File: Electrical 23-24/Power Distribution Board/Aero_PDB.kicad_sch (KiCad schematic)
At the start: 8 parts, among them J101 Conn_02x13_Top_Bottom

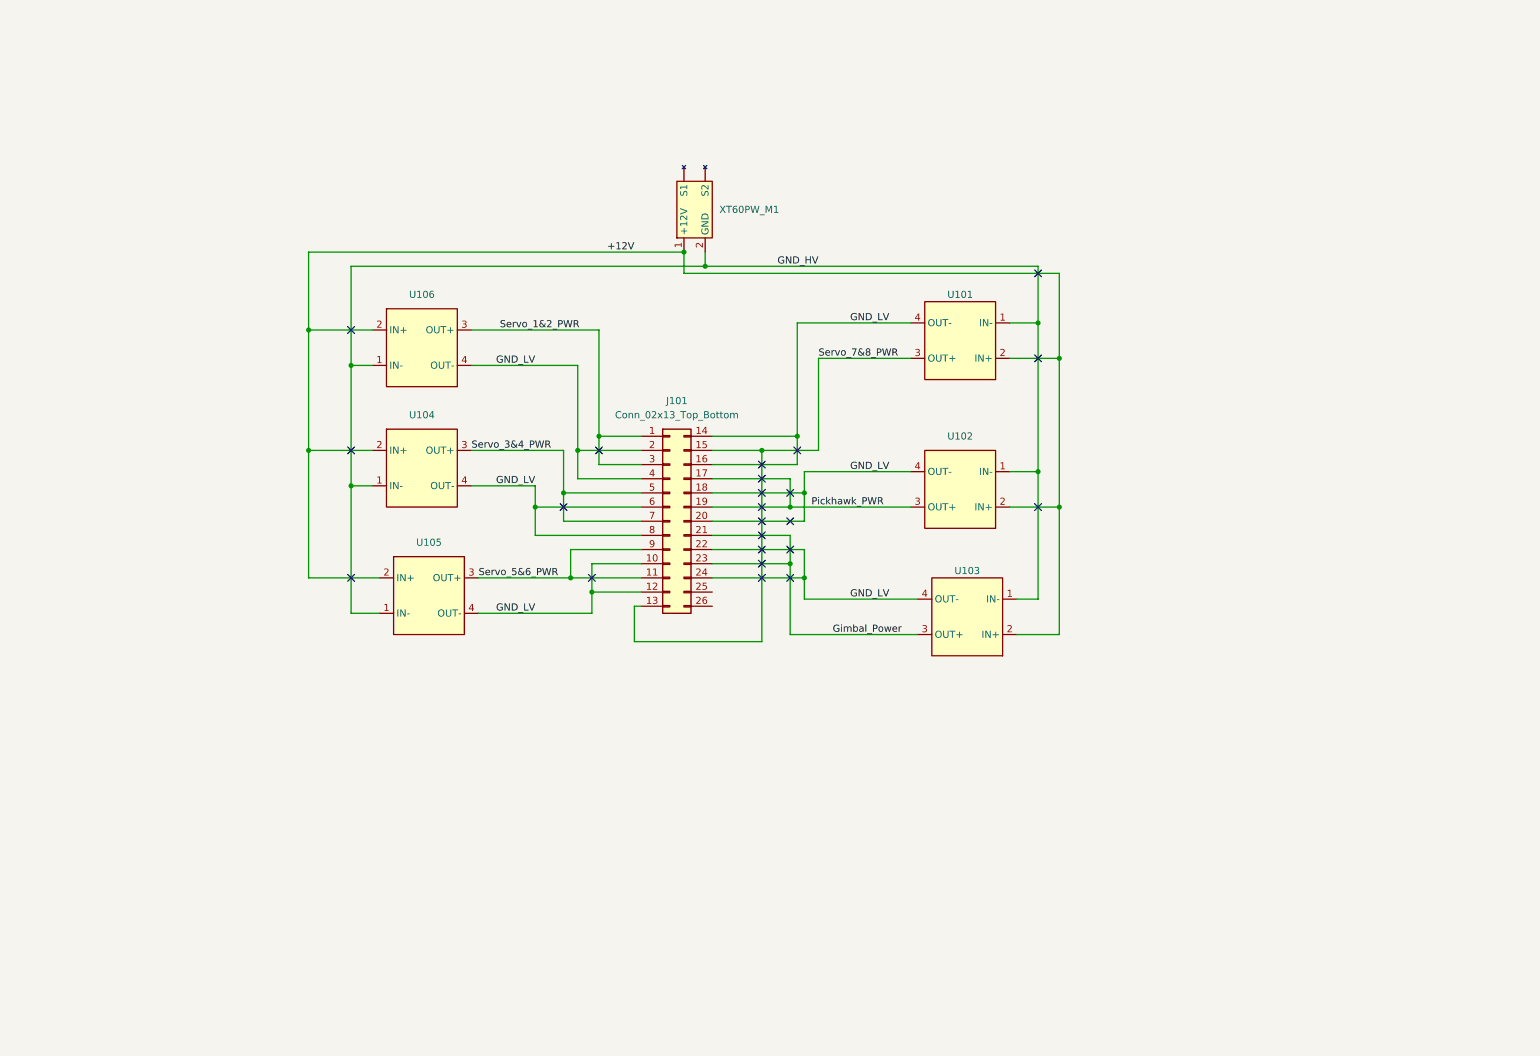
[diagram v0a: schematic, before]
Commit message: Updates to the PDB Design
Pushed Some Buck Converters to the back 
Added more connectors (for RasPi, Bullet, etc.)
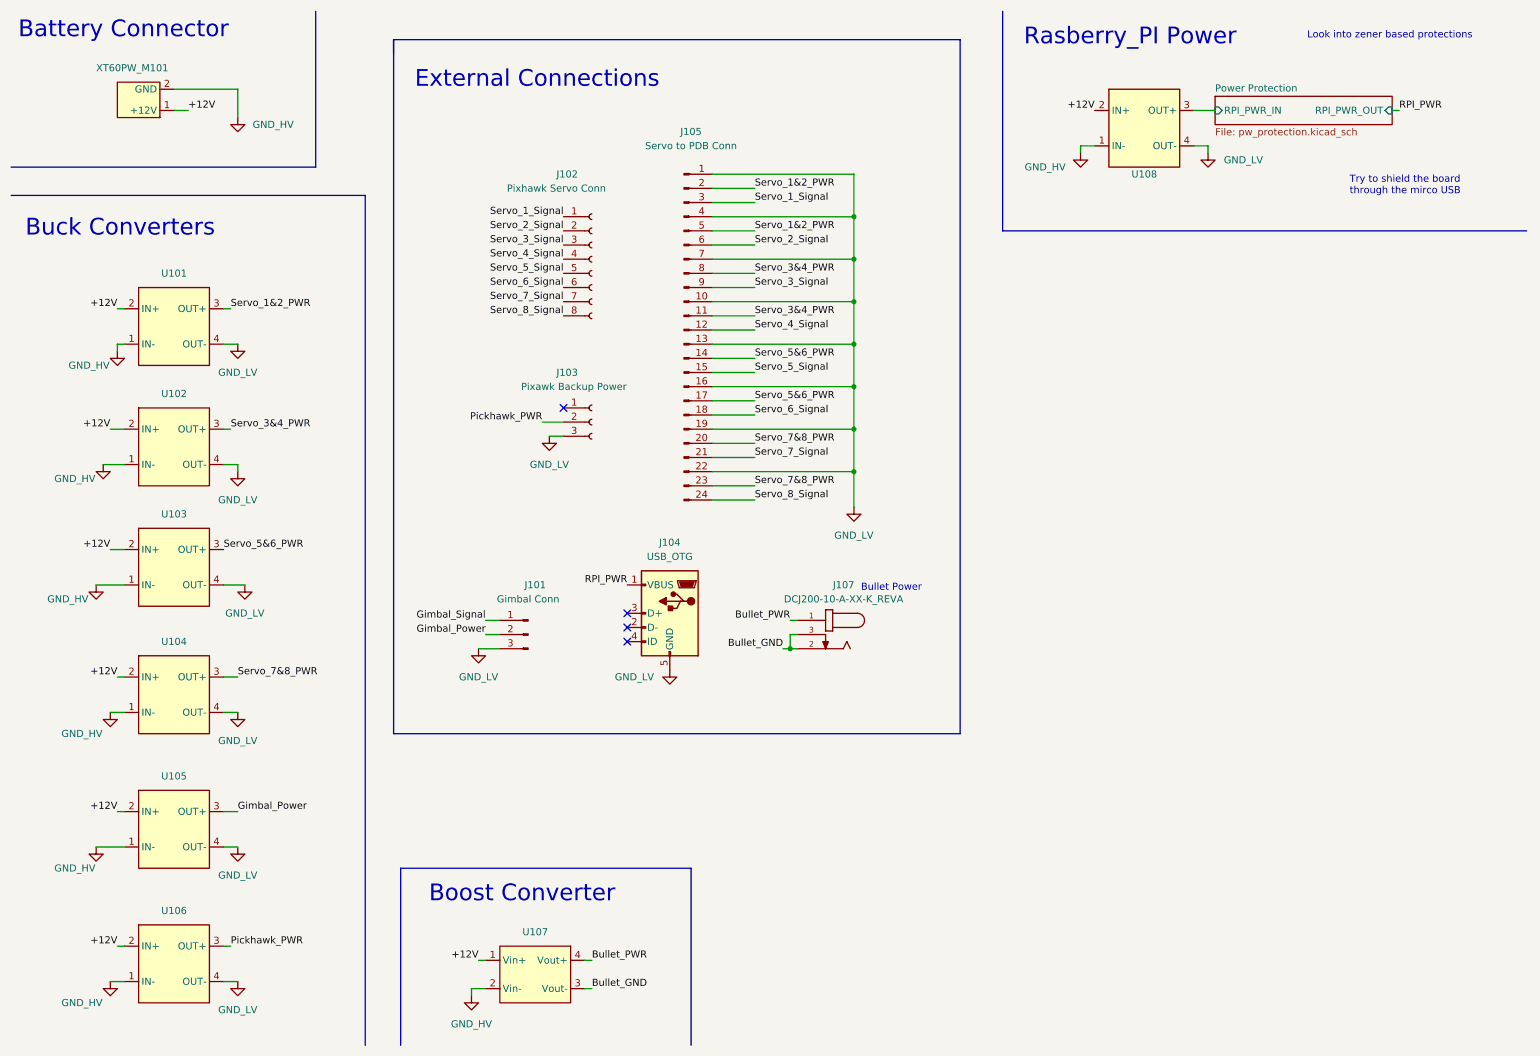
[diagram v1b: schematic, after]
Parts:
- removed J101: Conn_02x13_Top_Bottom, Connector_PinHeader_2.54mm:PinHeader_2x13_P2.54mm_Horizontal, symbol Connector_Generic:Conn_02x13_Top_Bottom
- added J101: Gimbal Conn, Connector_JST:JST_EH_B3B-EH-A_1x03_P2.50mm_Vertical, symbol Connector:Conn_01x03_Pin
- added J102: Pixhawk Servo Conn, Aero_PDB:CONN8_LFBN-RC_SUL, symbol Connector:Conn_01x08_Socket
- added J103: Pixawk Backup Power, Aero_PDB:SAMTEC_DW-03-XX-X-S-XXX, symbol Connector:Conn_01x03_Socket
- added J104: USB_OTG, Aero_PDB:MOLEX_47346-0001, symbol Connector:USB_OTG
- added J105: Servo to PDB Conn, Aero_PDB:SAMTEC_TSW-108-08-L-T-RA, symbol Connector:Conn_01x24_Pin
- added J107: DCJ200-10-A-XX-K_REVA, Aero_PDB:GCT_DCJ200-10-A-XX-K_REVA, symbol Aero_PDB_parts:DCJ200-10-A-XX-K_REVA
- added U107: ~, Aero_PDB:MT3608_module, symbol Aero_PDB_parts:MT3608_Boost_
- added U108: ~, Aero_PDB:YAAJ_DCDC_StepDown_LM2596, symbol Aero_PDB_parts:LM2596
- renumbered U106 to U101, U104 to U102, U105 to U103, U101 to U104, U103 to U105, U102 to U106, XT60PW_M1 to XT60PW_M101
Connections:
- net GND_LV is gone; now on net GND: U101.4 (OUT-), U102.4 (OUT-), U103.4 (OUT-), U104.4 (OUT-), U105.4 (OUT-), U106.4 (OUT-)
- net +12V: now also U107.1 (Vin+), U108.2 (IN+)
- net Gimbal_Power: now also J101.2 (Pin_2)
- net Pickhawk_PWR: now also J103.2 (Pin_2)
- net Servo_1&2_PWR: now also J105.2 (Pin_2), J105.5 (Pin_5)
- net Servo_3&4_PWR: now also J105.11 (Pin_11), J105.8 (Pin_8)
- net Servo_5&6_PWR: now also J105.14 (Pin_14), J105.17 (Pin_17)
- net Servo_7&8_PWR: now also J105.20 (Pin_20), J105.23 (Pin_23)
- net GND_HV renamed GND
- net GND: now also J101.3 (Pin_3), J104.5 (GND), J105.1 (Pin_1), J105.10 (Pin_10), J105.13 (Pin_13), J105.16 (Pin_16), J105.19 (Pin_19), J105.22 (Pin_22), J105.4 (Pin_4), J105.7 (Pin_7), U107.2 (Vin-), U108.4 (OUT-)
- new net Bullet_GND : J107.2, J107.3, U107.3 (Vout-)
- new net Bullet_PWR: J107.1, U107.4 (Vout+)
- new net GND1: U108.1 (IN-)
- new net GND2: J103.3 (Pin_3)
- new net Gimbal_Signal: J101.1 (Pin_1)
- new net Power Protection /RPI_PWR_IN: U108.3 (OUT+)
- new net RPI_PWR: J104.1 (VBUS)
- new net Servo_1_Signal: J102.1 (Pin_1), J105.3 (Pin_3)
- new net Servo_2_Signal: J102.2 (Pin_2), J105.6 (Pin_6)
- new net Servo_3_Signal: J102.3 (Pin_3), J105.9 (Pin_9)
- new net Servo_4_Signal: J102.4 (Pin_4), J105.12 (Pin_12)
- new net Servo_5_Signal: J102.5 (Pin_5), J105.15 (Pin_15)
- new net Servo_6_Signal: J102.6 (Pin_6), J105.18 (Pin_18)
- new net Servo_7_Signal: J102.7 (Pin_7), J105.21 (Pin_21)
- new net Servo_8_Signal: J102.8 (Pin_8), J105.24 (Pin_24)
- no-connect marks 23 -> 4
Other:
- added sheet Power Protection  (pw_protection.kicad_sch)
- note added: "Battery Connector"
- note added: "Boost Converter"
- note added: "Buck Converters"
- note added: "Bullet Power"
- note added: "External Connections"
- note added: "Look into zener based protections"
- note added: "Rasberry_PI Power"
- note added: "Try to shield the board through the mirco USB"
- moved on the sheet: U101, U102, U103, U104, U105, U106

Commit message: Final PDB (missing Aero Logo)
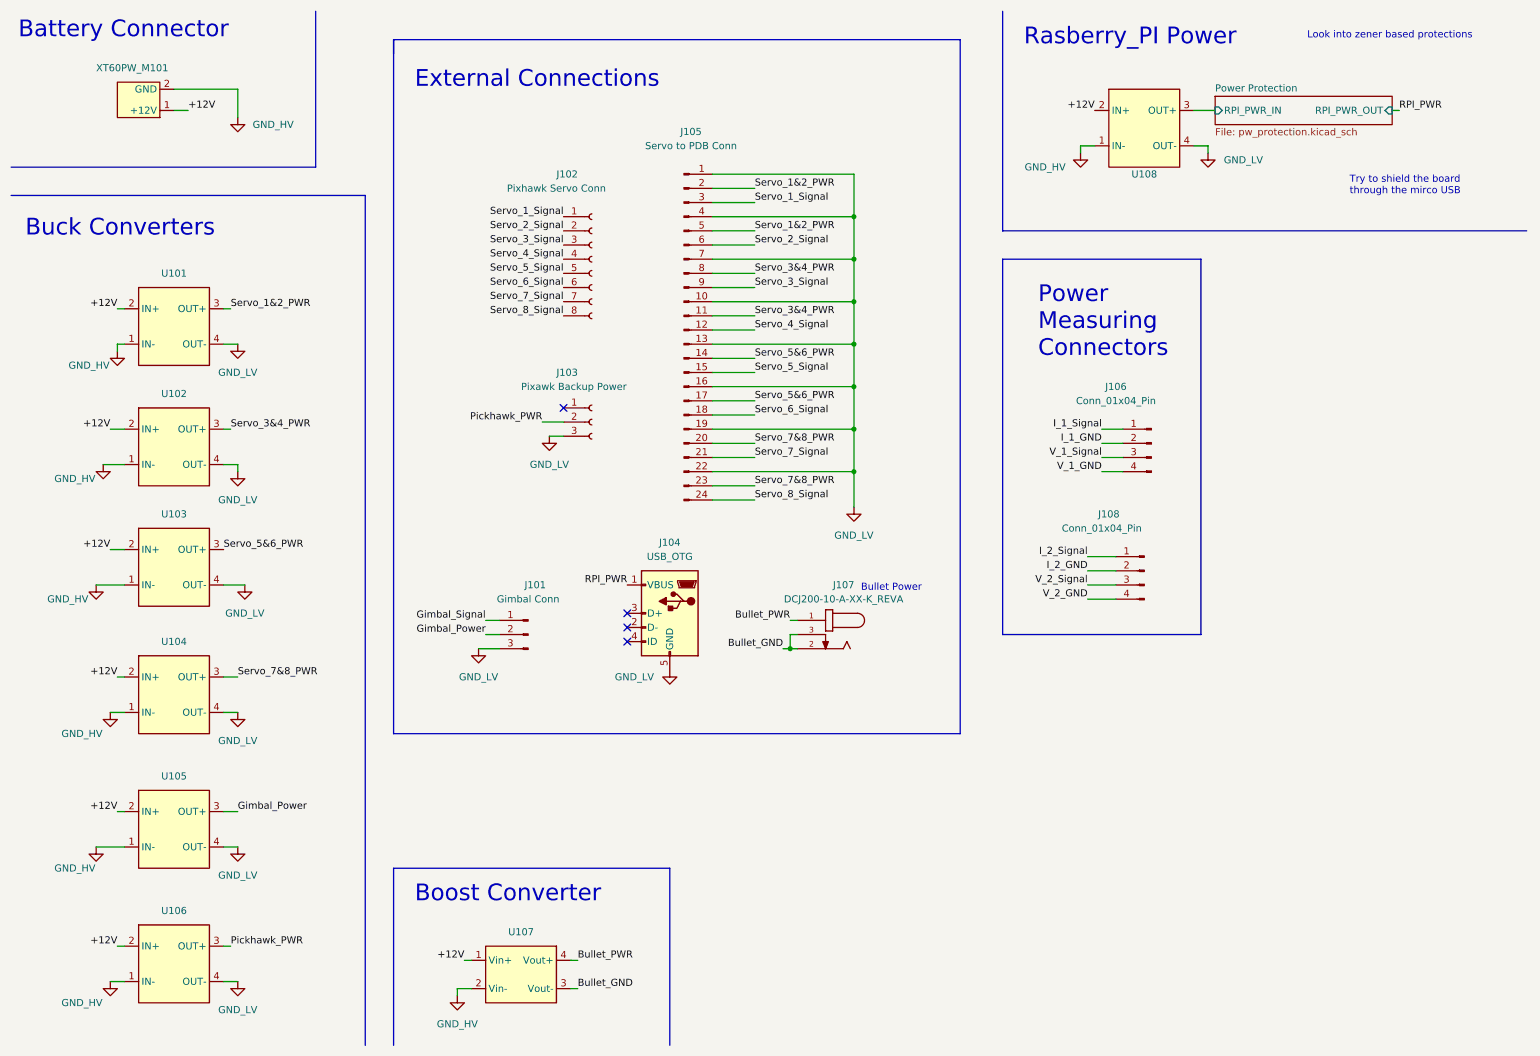
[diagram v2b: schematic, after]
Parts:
- added J106, J108: Conn_01x04_Pin, Connector_JST:JST_EH_B4B-EH-A_1x04_P2.50mm_Vertical, symbol Connector:Conn_01x04_Pin
- J102: footprint Aero_PDB:CONN8_LFBN-RC_SUL -> Connector_PinHeader_2.54mm:PinHeader_1x08_P2.54mm_Vertical
- J103: footprint Aero_PDB:SAMTEC_DW-03-XX-X-S-XXX -> Connector_PinHeader_2.54mm:PinHeader_1x03_P2.54mm_Vertical
- J105: footprint Aero_PDB:SAMTEC_TSW-108-08-L-T-RA -> Aero_PDB:SAMTEC_TSW-108-07-G-T
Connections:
- new net I_1_GND : J106.2 (Pin_2)
- new net I_1_Signal: J106.1 (Pin_1)
- new net I_2_GND : J108.2 (Pin_2)
- new net I_2_Signal: J108.1 (Pin_1)
- new net V_1_GND : J106.4 (Pin_4)
- new net V_1_Signal: J106.3 (Pin_3)
- new net V_2_GND : J108.4 (Pin_4)
- new net V_2_Signal: J108.3 (Pin_3)
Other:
- note added: "Power Measuring Connectors"
- moved on the sheet: U107

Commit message: Final Board
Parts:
- J106, J108: footprint Connector_JST:JST_EH_B4B-EH-A_1x04_P2.50mm_Vertical -> Connector_JST:JST_XH_B4B-XH-A_1x04_P2.50mm_Vertical
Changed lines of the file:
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@@
       (effects (font (size 1.27 1.27)))
     )
-    (property "Footprint" "Connector_JST:JST_EH_B4B-EH-A_1x04_P2.50mm_Vertical" (at 217.17 90.17 0)
+    (property "Footprint" "Connector_JST:JST_XH_B4B-XH-A_1x04_P2.50mm_Vertical" (at 217.17 90.17 0)
       (effects (font (size 1.27 1.27)) hide)
     )
@@
       (effects (font (size 1.27 1.27)))
     )
-    (property "Footprint" "Connector_JST:JST_EH_B4B-EH-A_1x04_P2.50mm_Vertical" (at 215.9 113.03 0)
+    (property "Footprint" "Connector_JST:JST_XH_B4B-XH-A_1x04_P2.50mm_Vertical" (at 215.9 113.03 0)
       (effects (font (size 1.27 1.27)) hide)
     )

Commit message: Finalize PDB board
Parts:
- added J1, J2: Conn_01x04_Pin, Connector_PinHeader_2.54mm:PinHeader_1x04_P2.54mm_Vertical, symbol Connector:Conn_01x04_Pin
- added J3, J4: RCIN, Connector_PinHeader_2.54mm:PinHeader_1x03_P2.54mm_Vertical, symbol Connector:Conn_01x03_Socket
- J101: footprint Connector_JST:JST_EH_B3B-EH-A_1x03_P2.50mm_Vertical -> Connector_JST:JST_EH_B2B-EH-A_1x02_P2.50mm_Vertical; symbol Connector:Conn_01x03_Pin -> Connector:Conn_01x02_Pin
- J106, J108: value Conn_01x04_Pin -> JST_XH_4
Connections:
- net GND2 is gone; now on net GND: J103.3 (Pin_3)
- net Gimbal_Signal is gone; now on net Gimbal_Power: J101.1 (Pin_1)
- net GND: now also J101.2 (Pin_2), J3.3 (Pin_3), J4.3 (Pin_3); no longer J101.3 (Pin_3), U101.1 (IN-), U102.1 (IN-), U103.1 (IN-), U104.1 (IN-), U105.1 (IN-), U106.1 (IN-), U107.2 (Vin-), XT60PW_M101.2 (GND)
- net GND1: now also U101.1 (IN-), U102.1 (IN-), U103.1 (IN-), U104.1 (IN-), U105.1 (IN-), U106.1 (IN-), U107.2 (Vin-), XT60PW_M101.2 (GND)
- net Gimbal_Power: no longer J101.2 (Pin_2)
- net I_1_GND : now also J106.4 (Pin_4), J2.4 (Pin_4); no longer J106.2 (Pin_2)
- net I_1_Signal: now also J106.3 (Pin_3), J2.3 (Pin_3); no longer J106.1 (Pin_1)
- net I_2_GND : now also J108.4 (Pin_4), J1.4 (Pin_4); no longer J108.2 (Pin_2)
- net I_2_Signal: now also J108.3 (Pin_3), J1.3 (Pin_3); no longer J108.1 (Pin_1)
- net V_1_GND : now also J106.2 (Pin_2), J2.2 (Pin_2); no longer J106.4 (Pin_4)
- net V_1_Signal: now also J106.1 (Pin_1), J2.1 (Pin_1); no longer J106.3 (Pin_3)
- net V_2_GND : now also J108.2 (Pin_2), J1.2 (Pin_2); no longer J108.4 (Pin_4)
- net V_2_Signal: now also J108.1 (Pin_1), J1.1 (Pin_1); no longer J108.3 (Pin_3)
- new net RCIN: J3.1 (Pin_1), J4.1 (Pin_1)
- no-connect marks 4 -> 6
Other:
- note added: "Radio Connector"

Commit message: Changing JST EH to JST XH connector for Gimbal
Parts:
- J101: footprint Connector_JST:JST_EH_B2B-EH-A_1x02_P2.50mm_Vertical -> Connector_JST:JST_XH_B2B-XH-A_1x02_P2.50mm_Vertical
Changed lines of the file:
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@@
       (effects (font (size 1.27 1.27)))
     )
-    (property "Footprint" "Connector_JST:JST_EH_B2B-EH-A_1x02_P2.50mm_Vertical" (at 105.41 124.46 0)
+    (property "Footprint" "Connector_JST:JST_XH_B2B-XH-A_1x02_P2.50mm_Vertical" (at 105.41 124.46 0)
       (effects (font (size 1.27 1.27)) hide)
     )
